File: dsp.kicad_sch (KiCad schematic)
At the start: 17 parts, among them IC106 CXD1167Q, X101 8.4672MHz

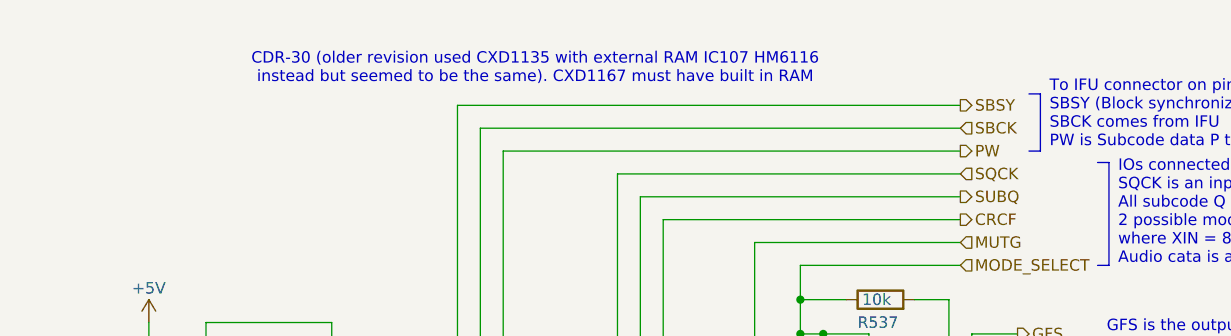
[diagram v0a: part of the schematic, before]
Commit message: Note added about DSP + external RAM also found in some CDR-30As. .gitattributes files added
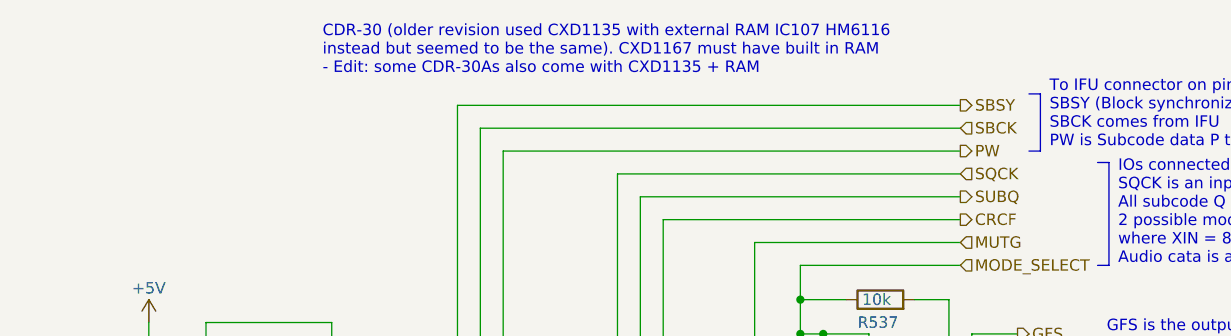
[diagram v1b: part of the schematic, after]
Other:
- note added: "CDR-30 (older revision used CXD1135 with external RAM IC107 HM6116 instead but seemed to be the same). CXD1167 must have built in RAM - Edit: some CDR-30As also come with CXD1135 + RAM"
- note removed: "CDR-30 (older revision used CXD1135 with external RAM IC107 HM6116 instead but seemed to be the same). CXD1167 must have built in RAM"
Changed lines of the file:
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@@
 		)
 	)
-	(text "CDR-30 (older revision used CXD1135 with external RAM IC107 HM6116\ninstead but seemed to be the same). CXD1167 must have built in RAM"
+	(text "CDR-30 (older revision used CXD1135 with external RAM IC107 HM6116\ninstead but seemed to be the same). CXD1167 must have built in RAM\n- Edit: some CDR-30As also come with CXD1135 + RAM"
 		(exclude_from_sim no)
-		(at 135.636 27.686 0)
+		(at 112.014 25.654 0)
 		(effects
 			(font
 				(size 1.27 1.27)
 			)
+			(justify left)
 		)
 	)

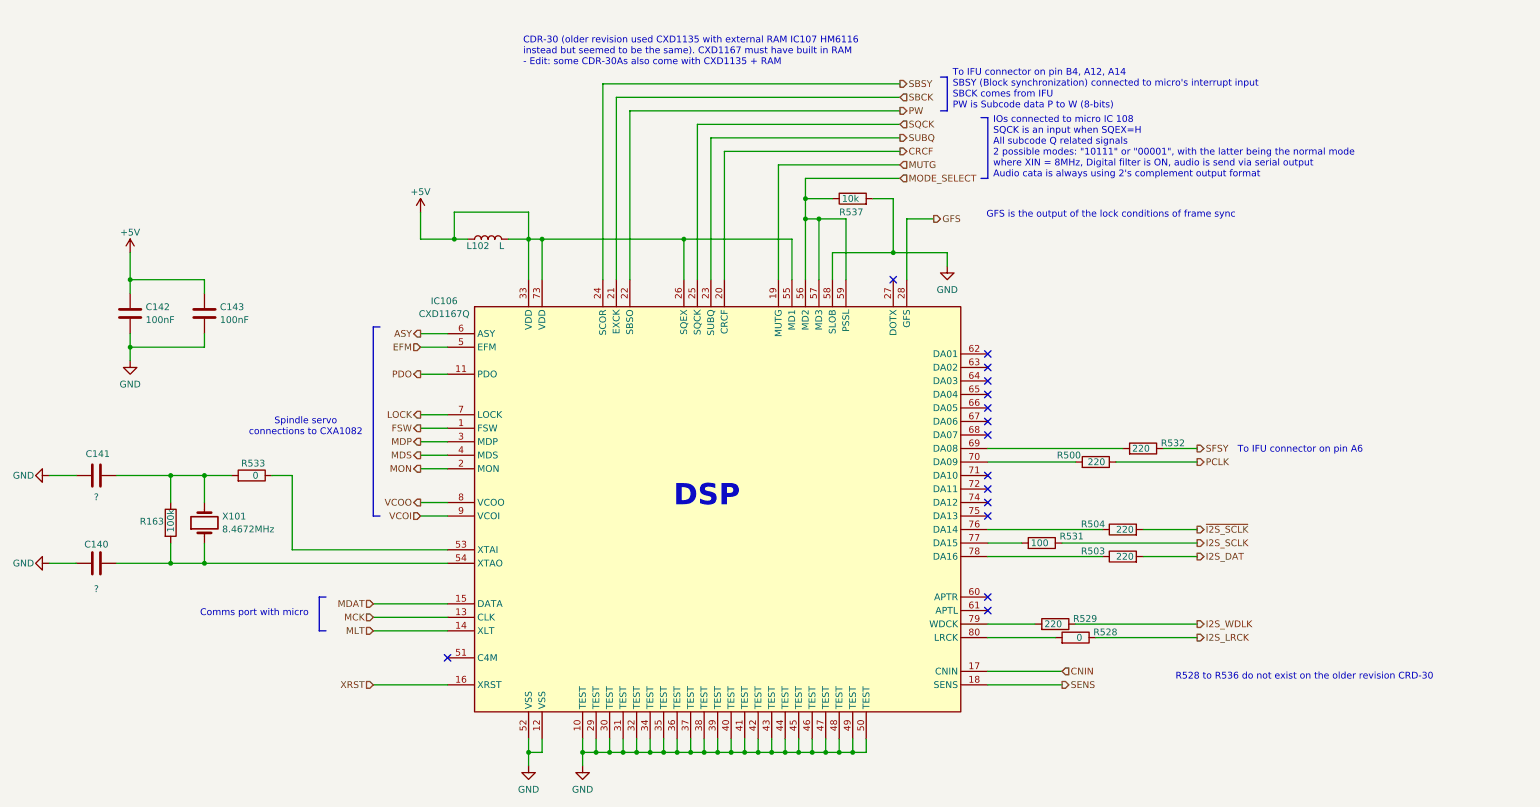
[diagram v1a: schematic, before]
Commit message: Small Schematics update to tidy signals attached to SCSI and MCU chips.
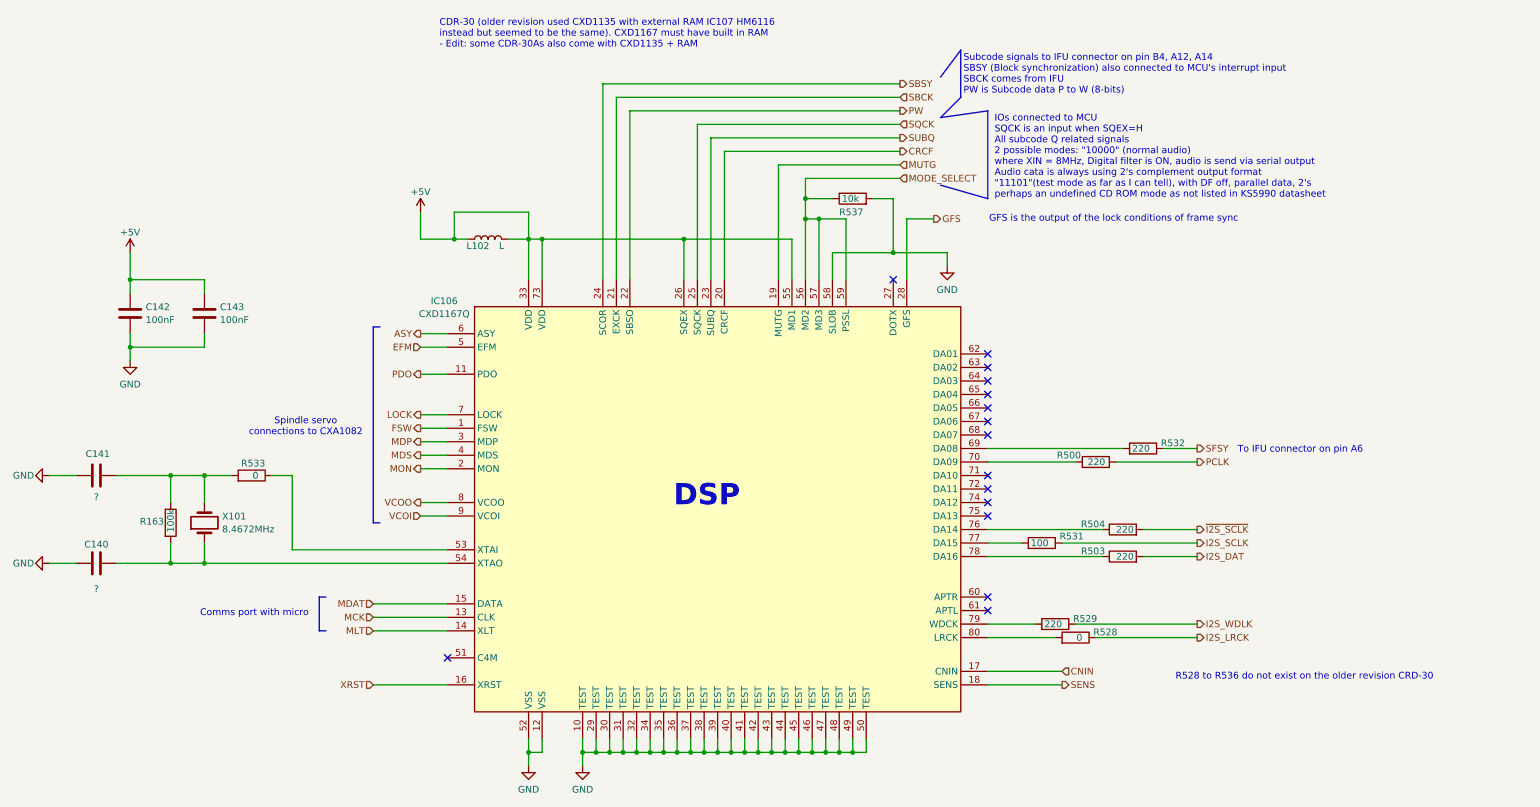
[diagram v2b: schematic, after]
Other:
- note added: "IOs connected to MCU SQCK is an input when SQEX=H All subcode Q related signals 2 possible modes: "10000" (normal audio) where XIN = 8MHz, Digital filter is ON, audio is send via serial output Audio cata is always using 2's complement output format "11101"(test mode as far as I can tell), with DF off, parallel data, 2's perhaps an undefined CD ROM mode as not listed in KS5990 datasheet"
- note added: "Subcode signals to IFU connector on pin B4, A12, A14 SBSY (Block synchronization) also connected to MCU's interrupt input SBCK comes from IFU PW is Subcode data P to W (8-bits)"
- note removed: "IOs connected to micro IC 108 SQCK is an input when SQEX=H All subcode Q related signals 2 possible modes: "10111" or "00001", with the latter being the normal mode where XIN = 8MHz, Digital filter is ON, audio is send via serial output Audio cata is always using 2's complement output format"
- note removed: "To IFU connector on pin B4, A12, A14 SBSY (Block synchronization) connected to micro's interrupt input SBCK comes from IFU PW is Subcode data P to W (8-bits)"
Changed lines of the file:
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@@
 	(title_block
 		(title "PC-Engine CDR-30A (CD-ROM2) Schematics - MAIN PWR")
-		(date "2024-05-03")
-		(rev "0.1")
+		(date "2024-07-19")
+		(rev "0.2")
 		(company "Author: Regis Galland")
 	)
@@
 	(polyline
 		(pts
-			(xy 199.39 38.1) (xy 199.39 49.53)
+			(xy 199.39 36.83) (xy 199.39 53.34)
 		)
 		(stroke
@@
 	(polyline
 		(pts
-			(xy 190.5 30.48) (xy 191.77 30.48)
+			(xy 190.5 30.48) (xy 194.31 25.4)
 		)
 		(stroke
@@
 	(polyline
 		(pts
-			(xy 191.77 30.48) (xy 191.77 36.83)
+			(xy 194.31 25.4) (xy 194.31 34.29)
 		)
 		(stroke
@@
 	(polyline
 		(pts
-			(xy 198.12 38.1) (xy 199.39 38.1)
+			(xy 190.5 38.1) (xy 199.39 36.83)
 		)
 		(stroke
@@
 	(polyline
 		(pts
-			(xy 198.12 49.53) (xy 199.39 49.53)
+			(xy 190.5 50.8) (xy 199.39 53.34)
 		)
 		(stroke
@@
 	(polyline
 		(pts
-			(xy 83.82 77.47) (xy 83.82 113.03)
+			(xy 83.82 77.47) (xy 83.82 114.3)
 		)
 		(stroke
@@
 	(polyline
 		(pts
-			(xy 190.5 36.83) (xy 191.77 36.83)
+			(xy 190.5 38.1) (xy 194.31 34.29)
 		)
 		(stroke
@@
 	(polyline
 		(pts
-			(xy 85.09 113.03) (xy 83.82 113.03)
+			(xy 85.09 114.3) (xy 83.82 114.3)
 		)
 		(stroke
@@
 	(text "GFS is the output of the lock conditions of frame sync"
 		(exclude_from_sim no)
-		(at 199.136 56.388 0)
+		(at 199.644 57.15 0)
 		(effects
 			(font
@@
 		)
 	)
-	(text "To IFU connector on pin B4, A12, A14\nSBSY (Block synchronization) connected to micro's interrupt input\nSBCK comes from IFU\nPW is Subcode data P to W (8-bits)"
+	(text "Subcode signals to IFU connector on pin B4, A12, A14\nSBSY (Block synchronization) also connected to MCU's interrupt input\nSBCK comes from IFU\nPW is Subcode data P to W (8-bits)"
 		(exclude_from_sim no)
-		(at 192.786 32.766 0)
+		(at 194.818 29.972 0)
 		(effects
 			(font
@@
 		)
 	)
-	(text "IOs connected to micro IC 108\nSQCK is an input when SQEX=H\nAll subcode Q related signals\n2 possible modes: \"10111\" or \"00001\", with the latter being the normal mode\nwhere XIN = 8MHz, Digital filter is ON, audio is send via serial output\nAudio cata is always using 2's complement output format\n"
+	(text "IOs connected to MCU\nSQCK is an input when SQEX=H\nAll subcode Q related signals\n2 possible modes: \"10000\" (normal audio)\nwhere XIN = 8MHz, Digital filter is ON, audio is send via serial output\nAudio cata is always using 2's complement output format\n\"11101\"(test mode as far as I can tell), with DF off, parallel data, 2's\nperhaps an undefined CD ROM mode as not listed in KS5990 datasheet\n"
 		(exclude_from_sim no)
-		(at 200.406 43.688 0)
+		(at 200.66 45.466 0)
 		(effects
 			(font
@@
 	(text "CDR-30 (older revision used CXD1135 with external RAM IC107 HM6116\ninstead but seemed to be the same). CXD1167 must have built in RAM\n- Edit: some CDR-30As also come with CXD1135 + RAM"
 		(exclude_from_sim no)
-		(at 112.014 25.654 0)
+		(at 96.266 22.352 0)
 		(effects
 			(font

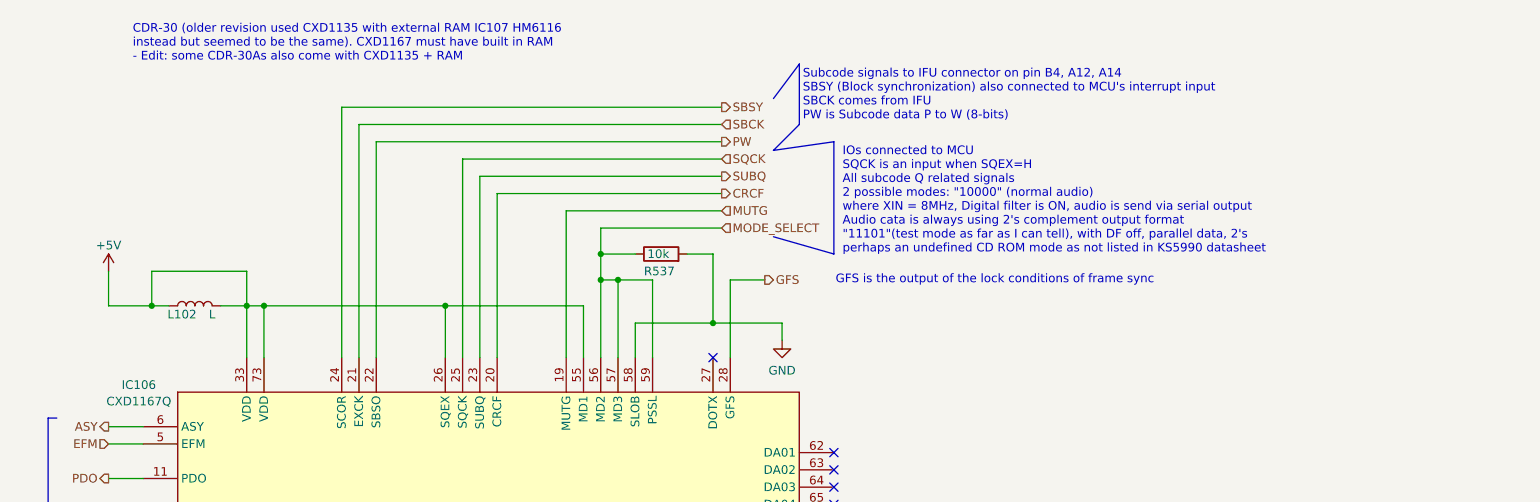
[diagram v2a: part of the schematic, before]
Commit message: KSS-220A Flexible PCBs ready and on order for trial.
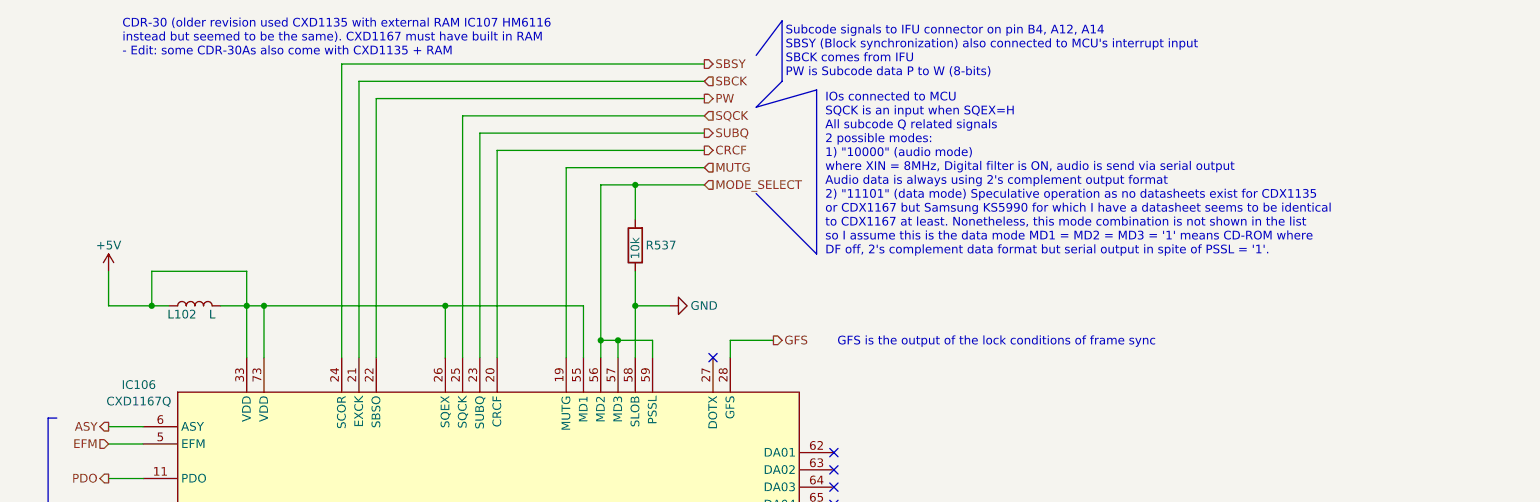
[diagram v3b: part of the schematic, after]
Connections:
- net GND: now also R537.1; no longer R537.2
- net MODE_SELECT: now also R537.2; no longer R537.1
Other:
- note added: "IOs connected to MCU SQCK is an input when SQEX=H All subcode Q related signals 2 possible modes: 1) "10000" (audio mode) where XIN = 8MHz, Digital filter is ON, audio is send via serial output Audio data is always using 2's complement output format 2) "11101" (data mode) Speculative operation as no datasheets exist for CDX1135 or CDX1167 but Samsung KS5990 for which I have a datasheet seems to b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"
- note removed: "IOs connected to MCU SQCK is an input when SQEX=H All subcode Q related signals 2 possible modes: "10000" (normal audio) where XIN = 8MHz, Digital filter is ON, audio is send via serial output Audio cata is always using 2's complement output format "11101"(test mode as far as I can tell), with DF off, parallel data, 2's perhaps an undefined CD ROM mode as not listed in KS5990 datasheet"
- moved on the sheet: R537
